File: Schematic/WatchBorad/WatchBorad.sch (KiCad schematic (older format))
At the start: 13 parts, among them IC1 TXS0108E, J1 Conn_01x06_Male, J2 Conn_01x09_Female, U1 E73-2G4M04S-52832, U2 FH26-13S-0.3SHW(05), U3 W25Q16BVSSIG

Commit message: Added Framebuffer keeper [SPI REFACTORING]
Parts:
- added C4, C5, C6: C, Capacitor_SMD:C_0805_2012Metric_Pad1.15x1.40mm_HandSolder, symbol Device:C
- added U4: BU6655NUX-TR, BU6655NUX-TR:SON50P200X300X60-9N, symbol BU6655NUX-TR:BU6655NUX-TR
- gave numbers to parts that had none: 2
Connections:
- wire segments 94 -> 113
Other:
- moved on the sheet: D1, R3
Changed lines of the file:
@@
-$EndComp
-$Comp
-L power:GND #PWR0114
-U 1 1 5DA8E6D3
-P 10700 4050
-F 0 "#PWR0114" H 10700 3800 50  0001 C CNN
-F 1 "GND" H 10705 3877 50  0000 C CNN
-F 2 "" H 10700 4050 50  0001 C CNN
-F 3 "" H 10700 4050 50  0001 C CNN
-	1    10700 4050
-	1    0    0    -1
 $EndComp
 $Comp
@@
 Wire Wire Line
 	10350 3950 10350 4050
-$Comp
-L power:GND #PWR0116
-U 1 1 5DA99CB6
-P 10350 4050
-F 0 "#PWR0116" H 10350 3800 50  0001 C CNN
-F 1 "GND" H 10355 3877 50  0000 C CNN
-F 2 "" H 10350 4050 50  0001 C CNN
-F 3 "" H 10350 4050 50  0001 C CNN
-	1    10350 4050
-	1    0    0    -1
-$EndComp
 Wire Wire Line
 	10700 3550 10700 3650
@@
 	3750 3850 3500 3850
 $Comp
-L Device:R R?
+L Device:R R3
 U 1 1 5DB1F5A6
-P 3350 6900
-F 0 "R?" V 3557 6900 50  0000 C CNN
-F 1 "1.5K" V 3466 6900 50  0000 C CNN
-F 2 "Resistor_SMD:R_0805_2012Metric_Pad1.15x1.40mm_HandSolder" V 3280 6900 50  0001 C CNN
-F 3 "~" H 3350 6900 50  0001 C CNN
-	1    3350 6900
+P 3200 6850
+F 0 "R3" V 3407 6850 50  0000 C CNN
+F 1 "1.5K" V 3316 6850 50  0000 C CNN
+F 2 "Resistor_SMD:R_0805_2012Metric_Pad1.15x1.40mm_HandSolder" V 3130 6850 50  0001 C CNN
+F 3 "~" H 3200 6850 50  0001 C CNN
+	1    3200 6850
 	0    -1   -1   0
 $EndComp
 $Comp
-L Device:LED D?
+L Device:LED D1
 U 1 1 5DB1F78E
-P 3750 6900
-F 0 "D?" H 3742 6645 50  0000 C CNN
-F 1 "LED" H 3742 6736 50  0000 C CNN
-F 2 "LED_SMD:LED_0805_2012Metric_Pad1.15x1.40mm_HandSolder" H 3750 6900 50  0001 C CNN
-F 3 "~" H 3750 6900 50  0001 C CNN
-	1    3750 6900
+P 3600 6850
+F 0 "D1" H 3592 6595 50  0000 C CNN
+F 1 "LED" H 3592 6686 50  0000 C CNN
+F 2 "LED_SMD:LED_0805_2012Metric_Pad1.15x1.40mm_HandSolder" H 3600 6850 50  0001 C CNN
+F 3 "~" H 3600 6850 50  0001 C CNN
+	1    3600 6850
 	-1   0    0    1
 $EndComp
 $Comp
-L power:GND #PWR?
+L power:GND #PWR0122
 U 1 1 5DB1F81C
-P 4000 7050
-F 0 "#PWR?" H 4000 6800 50  0001 C CNN
-F 1 "GND" H 4005 6877 50  0000 C CNN
-F 2 "" H 4000 7050 50  0001 C CNN
-F 3 "" H 4000 7050 50  0001 C CNN
-	1    4000 7050
-	1    0    0    -1
-$EndComp
-Wire Wire Line
-	3900 6900 4000 6900
-Wire Wire Line
-	4000 6900 4000 7050
-Wire Wire Line
-	3600 6900 3500 6900
-Text Label 3200 6900 2    50   ~ 0
+P 3850 7000
+F 0 "#PWR0122" H 3850 6750 50  0001 C CNN
+F 1 "GND" H 3855 6827 50  0000 C CNN
+F 2 "" H 3850 7000 50  0001 C CNN
+F 3 "" H 3850 7000 50  0001 C CNN
+	1    3850 7000
+	1    0    0    -1
+$EndComp
+Wire Wire Line
+	3750 6850 3850 6850
+Wire Wire Line
+	3850 6850 3850 7000
+Wire Wire Line
+	3450 6850 3350 6850
+Text Label 3050 6850 2    50   ~ 0
 BRD_LED_P13
 Wire Wire Line
@@
 Text Label 3750 2650 0    50   ~ 0
 BRD_LED_P13
+$Comp
+L BU6655NUX-TR:BU6655NUX-TR U4
+U 1 1 5DB2A27E
+P 5050 7000
+F 0 "U4" H 5050 7567 50  0000 C CNN
+F 1 "BU6655NUX-TR" H 5050 7476 50  0000 C CNN
+F 2 "BU6655NUX-TR:SON50P200X300X60-9N" H 5050 7000 50  0001 L BNN
+F 3 "LDO Regulator POS 3.3V/2.8V/1.8V 0.2A 8-Pin VSON Embossed T/R" H 5050 7000 50  0001 L BNN
+F 4 "BU6655NUXCT-ND" H 5050 7000 50  0001 L BNN "Field4"
+F 5 "BU6655NUX-TR" H 5050 7000 50  0001 L BNN "Field5"
+F 6 "UFDFN-8 Rohm" H 5050 7000 50  0001 L BNN "Field6"
+F 7 "Rohm" H 5050 7000 50  0001 L BNN "Field7"
+F 8 "https://www.digikey.com/product-detail/en/rohm-semiconductor/BU6655NUX-TR/BU6655NUXCT-ND/4626053?utm_source=snapeda&utm_medium=aggregator&utm_campaign=symbol" H 5050 7000 50  0001 L BNN "Field8"
+	1    5050 7000
+	1    0    0    -1
+$EndComp
+$Comp
+L power:+3.3V #PWR0123
+U 1 1 5DB2A8BB
+P 5900 6900
+F 0 "#PWR0123" H 5900 6750 50  0001 C CNN
+F 1 "+3.3V" H 5915 7073 50  0000 C CNN
+F 2 "" H 5900 6900 50  0001 C CNN
+F 3 "" H 5900 6900 50  0001 C CNN
+	1    5900 6900
+	1    0    0    -1
+$EndComp
+$Comp
+L power:+2V8 #PWR0124
+U 1 1 5DB319AF
+P 6250 6950
+F 0 "#PWR0124" H 6250 6800 50  0001 C CNN
+F 1 "+2V8" H 6265 7123 50  0000 C CNN
+F 2 "" H 6250 6950 50  0001 C CNN
+F 3 "" H 6250 6950 50  0001 C CNN
+	1    6250 6950
+	1    0    0    -1
+$EndComp
+$Comp
+L power:+1V8 #PWR0125
+U 1 1 5DB38F15
+P 6600 7000
+F 0 "#PWR0125" H 6600 6850 50  0001 C CNN
+F 1 "+1V8" H 6615 7173 50  0000 C CNN
+F 2 "" H 6600 7000 50  0001 C CNN
+F 3 "" H 6600 7000 50  0001 C CNN
+	1    6600 7000
+	1    0    0    -1
+$EndComp
+Wire Wire Line
+	5550 6900 5900 6900
+Wire Wire Line
+	5550 7300 5650 7300
+Wire Wire Line
+	5650 7300 5650 7450
+$Comp
+L power:GND #PWR0114
+U 1 1 5DB58294
+P 5650 7450
+F 0 "#PWR0114" H 5650 7200 50  0001 C CNN
+F 1 "GND" H 5655 7277 50  0000 C CNN
+F 2 "" H 5650 7450 50  0001 C CNN
+F 3 "" H 5650 7450 50  0001 C CNN
+	1    5650 7450
+	1    0    0    -1
+$EndComp
+$Comp
+L Device:C C4
+U 1 1 5DB58357
+P 5900 7300
+F 0 "C4" H 6015 7346 50  0000 L CNN
+F 1 "C" H 6015 7255 50  0000 L CNN
+F 2 "Capacitor_SMD:C_0805_2012Metric_Pad1.15x1.40mm_HandSolder" H 5938 7150 50  0001 C CNN
+F 3 "~" H 5900 7300 50  0001 C CNN
+	1    5900 7300
+	1    0    0    -1
+$EndComp
+$Comp
+L Device:C C5
+U 1 1 5DB583B2
+P 6250 7300
+F 0 "C5" H 6365 7346 50  0000 L CNN
+F 1 "C" H 6365 7255 50  0000 L CNN
+F 2 "Capacitor_SMD:C_0805_2012Metric_Pad1.15x1.40mm_HandSolder" H 6288 7150 50  0001 C CNN
+F 3 "~" H 6250 7300 50  0001 C CNN
+	1    6250 7300
+	1    0    0    -1
+$EndComp
+$Comp
+L Device:C C6
+U 1 1 5DB58419
+P 6600 7300
+F 0 "C6" H 6715 7346 50  0000 L CNN
+F 1 "C" H 6715 7255 50  0000 L CNN
+F 2 "Capacitor_SMD:C_0805_2012Metric_Pad1.15x1.40mm_HandSolder" H 6638 7150 50  0001 C CNN
+F 3 "~" H 6600 7300 50  0001 C CNN
+	1    6600 7300
+	1    0    0    -1
+$EndComp
+Wire Wire Line
+	5900 7150 5900 6900
+Connection ~ 5900 6900
+Wire Wire Line
+	6250 7000 6250 6950
+Wire Wire Line
+	5550 7000 6250 7000
+Wire Wire Line
+	6250 7000 6250 7150
+Connection ~ 6250 7000
+Wire Wire Line
+	6600 7000 6600 7100
+Connection ~ 6600 7100
+Wire Wire Line
+	6600 7100 6600 7150
+Wire Wire Line
+	5550 7100 6600 7100
+Wire Wire Line
+	5900 7450 5900 7500
+Wire Wire Line
+	5900 7500 6250 7500
+Wire Wire Line
+	6250 7500 6250 7450
+Wire Wire Line
+	6250 7500 6600 7500
+Wire Wire Line
+	6600 7500 6600 7450
+Connection ~ 6250 7500
+$Comp
+L power:GND #PWR0116
+U 1 1 5DB87B90
+P 6250 7550
+F 0 "#PWR0116" H 6250 7300 50  0001 C CNN
+F 1 "GND" H 6255 7377 50  0000 C CNN
+F 2 "" H 6250 7550 50  0001 C CNN
+F 3 "" H 6250 7550 50  0001 C CNN
+	1    6250 7550
+	1    0    0    -1
+$EndComp
+Wire Wire Line
+	6250 7500 6250 7550
+Wire Wire Line
+	10350 4050 10550 4050
+$Comp
+L power:GND #PWR0126
+U 1 1 5DB9DB9C
+P 10550 4150
+F 0 "#PWR0126" H 10550 3900 50  0001 C CNN
+F 1 "GND" H 10555 3977 50  0000 C CNN
+F 2 "" H 10550 4150 50  0001 C CNN
+F 3 "" H 10550 4150 50  0001 C CNN
+	1    10550 4150
+	1    0    0    -1
+$EndComp
+Wire Wire Line
+	10550 4150 10550 4050
+Connection ~ 10550 4050
+Wire Wire Line
+	10550 4050 10700 4050
 $EndSCHEMATC

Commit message: Started work on BLE driver [BLE, UNTESTED]
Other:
- note added: "Onboard RED LED"
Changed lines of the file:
@@
 Wire Wire Line
 	10550 4050 10700 4050
+Wire Notes Line
+	2500 6300 2500 7700
+Wire Notes Line
+	2500 7700 4100 7700
+Wire Notes Line
+	4100 7700 4100 6300
+Wire Notes Line
+	4100 6300 2500 6300
+Text Notes 2900 7550 0    50   ~ 0
+Onboard RED LED
 $EndSCHEMATC

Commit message: Moved footprints and symbol libraries to KICAD_LIBRARIES_ROOT
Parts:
- added U5: MCP1700-3302E_SOT23, Package_TO_SOT_SMD:SOT-23, symbol Regulator_Linear:MCP1700-3302E_SOT23
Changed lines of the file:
@@
 Connection ~ 6250 7000
-Wire Wire Line
-	6600 7000 6600 7100
-Connection ~ 6600 7100
-Wire Wire Line
-	6600 7100 6600 7150
 Wire Wire Line
 	5550 7100 6600 7100
@@
 Text Notes 2900 7550 0    50   ~ 0
 Onboard RED LED
+Connection ~ 6600 7100
+Wire Wire Line
+	6600 7100 6600 7150
+Wire Wire Line
+	6600 7000 6600 7100
+$Comp
+L Regulator_Linear:MCP1700-3302E_SOT23 U5
+U 1 1 5DBB69D4
+P 5050 6000
+F 0 "U5" H 5050 6242 50  0000 C CNN
+F 1 "MCP1700-3302E_SOT23" H 5050 6151 50  0000 C CNN
+F 2 "Package_TO_SOT_SMD:SOT-23" H 5050 6225 50  0001 C CNN
+F 3 "http://ww1.microchip.com/downloads/en/DeviceDoc/20001826C.pdf" H 5050 6000 50  0001 C CNN
+	1    5050 6000
+	1    0    0    -1
+$EndComp
 $EndSCHEMATC

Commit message: Draft of board route [PCB Routing]
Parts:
- removed C5, C6: C, Capacitor_SMD:C_0805_2012Metric_Pad1.15x1.40mm_HandSolder, symbol Device:C
- removed U4: BU6655NUX-TR, BU6655NUX-TR:SON50P200X300X60-9N, symbol BU6655NUX-TR:BU6655NUX-TR
- added C10, C11, C12, C13, C14, C16, C7, C8, C9: 0.1uF, Capacitor_SMD:C_0805_2012Metric_Pad1.15x1.40mm_HandSolder, symbol Device:C
- added C15: 10nF, Capacitor_SMD:C_0805_2012Metric_Pad1.15x1.40mm_HandSolder, symbol Device:C
- added F1: Polyfuse, Fuse:Fuse_1206_3216Metric_Pad1.42x1.75mm_HandSolder, symbol Device:Polyfuse
- added J3: USB_B_Mini, Connector_USB:USB_Mini-B_Lumberg_2486_01_Horizontal, symbol Connector:USB_B_Mini
- added J4: Conn_01x10_Female, Connector_PinSocket_2.54mm:PinSocket_1x10_P2.54mm_Vertical, symbol Connector:Conn_01x10_Female
- added J5: Conn_01x06_Female, Connector_PinSocket_2.54mm:PinSocket_1x06_P2.54mm_Vertical, symbol Connector:Conn_01x06_Female
- added J6: Conn_01x04_Male, Connector_PinHeader_2.54mm:PinHeader_1x04_P2.54mm_Vertical, symbol Connector:Conn_01x04_Male
- added R4, R5, R6: 4.7k, Resistor_SMD:R_0805_2012Metric_Pad1.15x1.40mm_HandSolder, symbol Device:R
- added R7: 3.3k, Resistor_SMD:R_0805_2012Metric_Pad1.15x1.40mm_HandSolder, symbol Device:R
- added R8, R9: 2k, Resistor_SMD:R_0805_2012Metric_Pad1.15x1.40mm_HandSolder, symbol Device:R
- added RESET, SW1, SW2: SW_Push, Button_Switch_SMD:SW_SPST_SKQG_WithStem, symbol Switch:SW_Push
- added U6: MCP1700-1802E_SOT23, Package_TO_SOT_SMD:SOT-23, symbol Regulator_Linear:MCP1700-1802E_SOT23
- added U7: LP2985-2.8, Package_TO_SOT_SMD:SOT-23-5, symbol Regulator_Linear:LP2985-2.8
- added U8: MPU-9250, QFN40P300X300X105-24N, symbol MPU-9250:MPU-9250
- C4: value C -> 0.1uF
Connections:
- net labels added: +5V, MPU_ADO, MPU_INT, MPU_SCLK, MPU_SDA, MPU_SYNC, UART1_RX, UART1_TX
- wire segments 113 -> 235
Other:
- note added: "Diplsay & board supply"
- note added: "Gyroscope & Accelerometer & Magnetometer with I2C interface"
- note added: "SPI FLASH Memory\n"
- moved on the sheet: C1, C2, C3, IC1, J2, R1, R2, U2, U3, U5

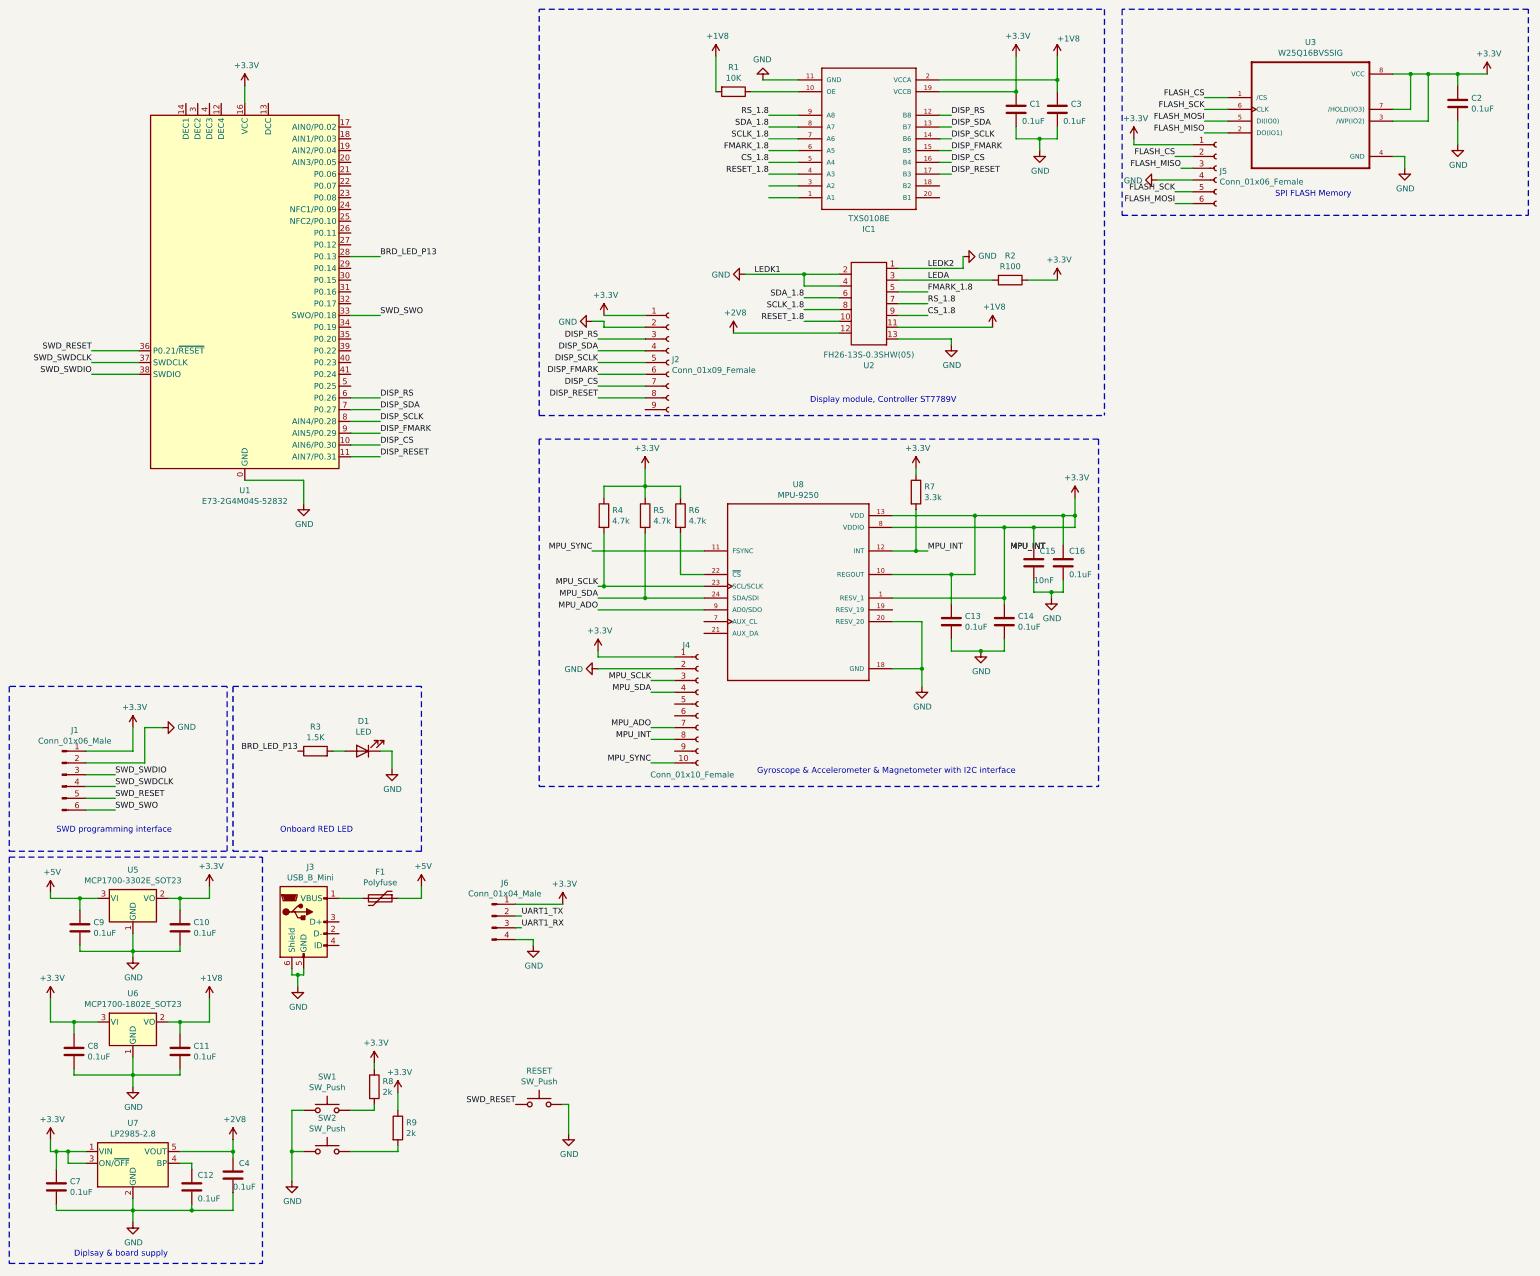
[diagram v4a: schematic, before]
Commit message: Updated board summary. Added borders and names for several schematic parts
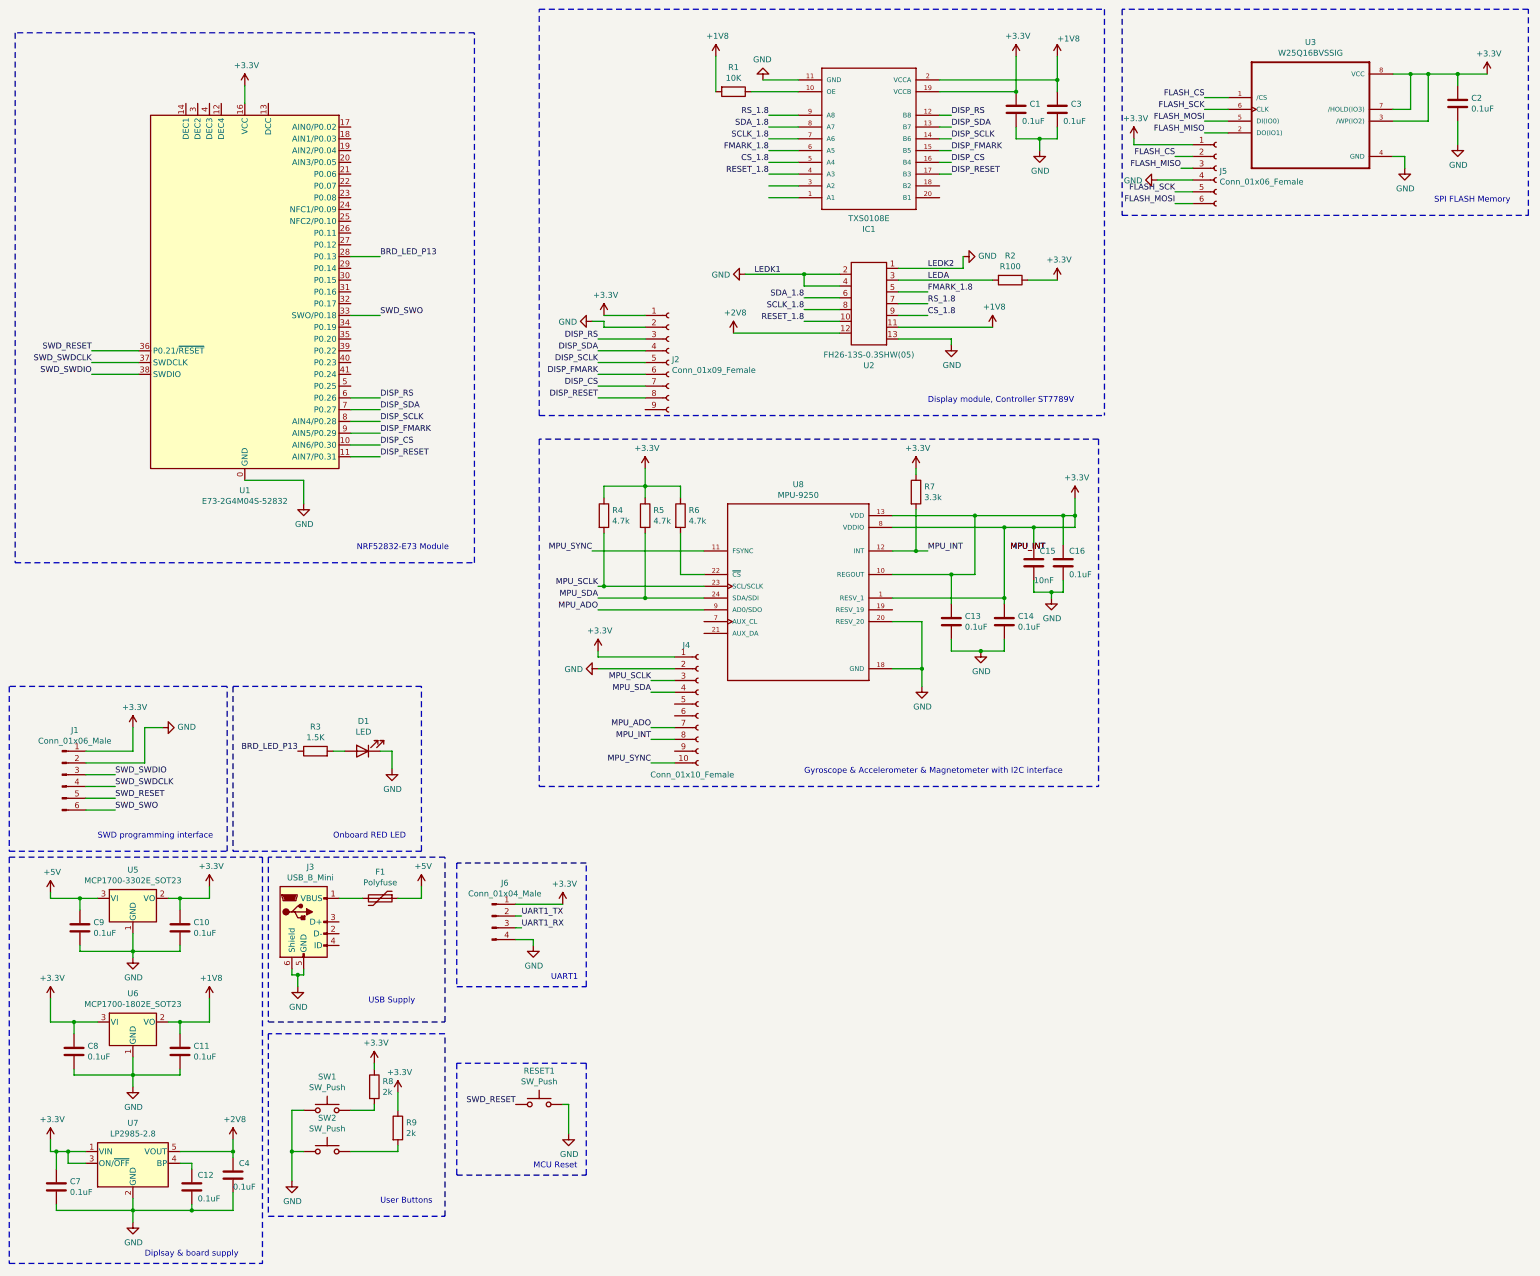
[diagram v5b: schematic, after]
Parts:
- renumbered RESET to RESET1
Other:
- note added: "MCU Reset"
- note added: "NRF52832-E73 Module"
- note added: "UART1"
- note added: "USB Supply"
- note added: "User Buttons"
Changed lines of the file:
@@
 Wire Wire Line
 	12900 1100 13150 1100
-Text Notes 7400 3900 0    50   ~ 0
+Text Notes 8400 3900 0    50   ~ 0
 Display module, Controller ST7789V
 $Comp
@@
 Wire Notes Line
 	600  6300 600  7700
-Text Notes 1000 7550 0    50   ~ 0
+Text Notes 1350 7600 0    50   ~ 0
 SWD programming interface
 Text Label 3750 4150 0    50   ~ 0
@@
 Wire Notes Line
 	4100 7700 4100 6300
-Text Notes 2900 7550 0    50   ~ 0
+Text Notes 3350 7600 0    50   ~ 0
 Onboard RED LED
 $Comp
@@
 	950  10250 950  10150
 Connection ~ 1000 10250
-Text Notes 1150 11150 0    50   ~ 0
+Text Notes 1750 11150 0    50   ~ 0
 Diplsay & board supply
 Wire Notes Line
@@
 Wire Notes Line
 	13500 550  10050 550
-Text Notes 11350 2150 0    50   ~ 0
+Text Notes 12700 2200 0    50   ~ 0
 SPI FLASH Memory\n
 $Comp
@@
 Wire Notes Line
 	9850 4200 5100 4200
-Text Notes 6950 7050 0    50   ~ 0
+Text Notes 7350 7050 0    50   ~ 0
 Gyroscope & Accelerometer & Magnetometer with I2C interface
 $Comp
@@
 	3000 10250 3000 10500
 $Comp
-L Switch:SW_Push RESET
-U 1 1 5E7B968E
-P 5100 9850
-F 0 "RESET" H 5100 10135 50  0000 C CNN
-F 1 "SW_Push" H 5100 10044 50  0000 C CNN
-F 2 "Button_Switch_SMD:SW_SPST_SKQG_WithStem" H 5100 10050 50  0001 C CNN
-F 3 "~" H 5100 10050 50  0001 C CNN
-	1    5100 9850
-	1    0    0    -1
-$EndComp
-$Comp
 L power:GND #PWR0148
 U 1 1 5E7BB451
@@
 Text Label 4900 9850 2    50   ~ 0
 SWD_RESET
+$Comp
+L Switch:SW_Push RESET1
+U 1 1 5E7B968E
+P 5100 9850
+F 0 "RESET1" H 5100 10135 50  0000 C CNN
+F 1 "SW_Push" H 5100 10044 50  0000 C CNN
+F 2 "Button_Switch_SMD:SW_SPST_SKQG_WithStem" H 5100 10050 50  0001 C CNN
+F 3 "~" H 5100 10050 50  0001 C CNN
+	1    5100 9850
+	1    0    0    -1
+$EndComp
+Wire Notes Line
+	4400 7800 4400 8850
+Wire Notes Line
+	4400 8850 5500 8850
+Wire Notes Line
+	5500 8850 5500 7800
+Wire Notes Line
+	5500 7800 4400 7800
+Text Notes 5200 8800 0    50   ~ 0
+UART1
+Wire Notes Line
+	2800 7750 2800 9150
+Wire Notes Line
+	2800 9150 4300 9150
+Wire Notes Line
+	4300 9150 4300 7750
+Wire Notes Line
+	4300 7750 2800 7750
+Text Notes 3650 9000 0    50   ~ 0
+USB Supply
+Wire Notes Line
+	2800 9250 2800 10800
+Wire Notes Line
+	2800 10800 4300 10800
+Wire Notes Line
+	4300 10800 4300 9250
+Wire Notes Line
+	4300 9250 2800 9250
+Text Notes 3750 10700 0    50   ~ 0
+User Buttons
+Wire Notes Line
+	4400 9500 4400 10450
+Wire Notes Line
+	4400 10450 5500 10450
+Wire Notes Line
+	5500 10450 5500 9500
+Wire Notes Line
+	5500 9500 4400 9500
+Text Notes 5050 10400 0    50   ~ 0
+MCU Reset
+Wire Notes Line
+	650  750  650  5250
+Wire Notes Line
+	650  5250 4550 5250
+Wire Notes Line
+	4550 5250 4550 750
+Wire Notes Line
+	4550 750  650  750
+Text Notes 3550 5150 0    50   ~ 0
+NRF52832-E73 Module
 $EndSCHEMATC
